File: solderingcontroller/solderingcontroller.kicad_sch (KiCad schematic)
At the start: 33 parts, among them J1 230V AC, Q3 BUZ11, Q4 BUZ11, SW1 HANDLE_DETECT, SW3 RotaryEncoder_Switch, T1 230/24, U1 ESP32-C3_SUPERMINI, U2 OLED LCD I2C, U3 16Bit I2C ADS1115 Module, U4 AMS1117-3.3, U6 VOM1271T, U7 4N25

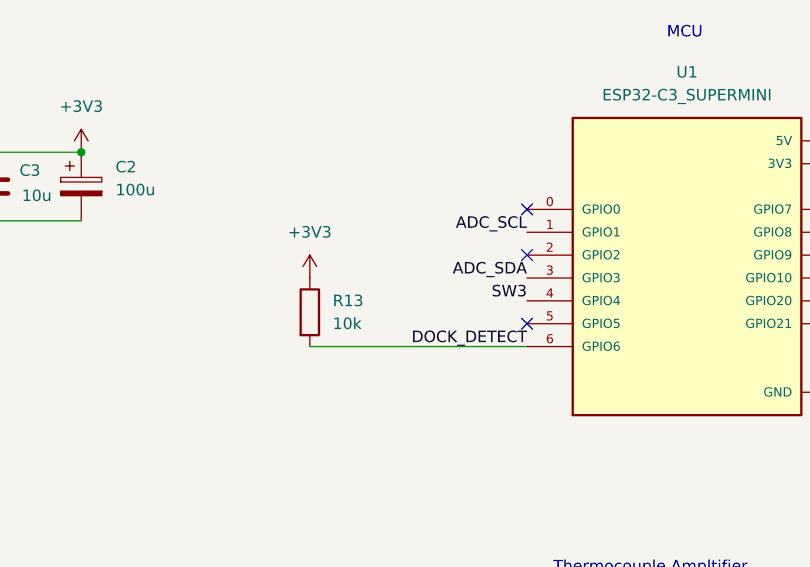
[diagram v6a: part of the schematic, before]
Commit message: Remove DOCK_DETECT PU
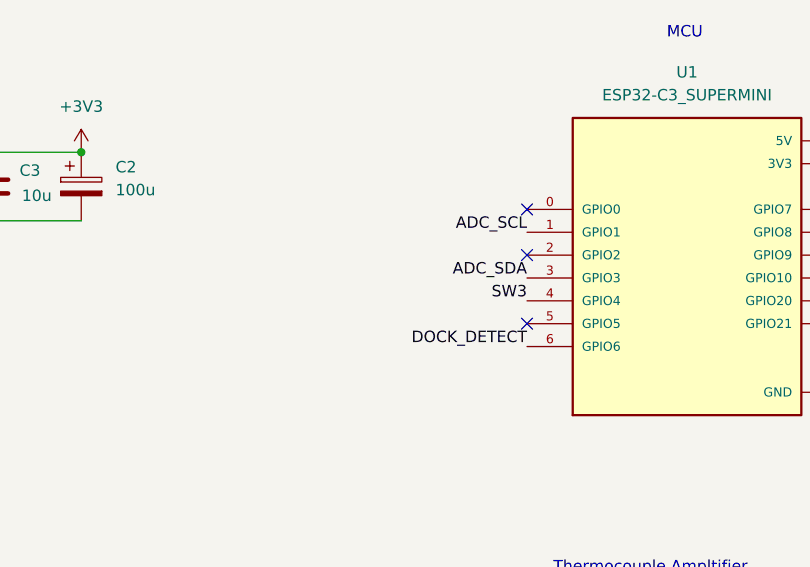
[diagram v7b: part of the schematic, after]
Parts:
- removed R13: 10k, symbol Device:R
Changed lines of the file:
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@@
 	(wire
 		(pts
-			(xy 86.36 52.07) (xy 110.49 52.07)
-		)
-		(stroke
-			(width 0)
-			(type default)
-		)
-	)
-	(wire
-		(pts
 			(xy 26.67 38.1) (xy 41.91 38.1)
 		)
@@
 	)
 	(symbol
-		(lib_id "Device:R")
-		(at 86.36 48.26 0)
-		(unit 1)
-		(exclude_from_sim no)
-		(in_bom yes)
-		(on_board yes)
-		(dnp no)
-		(fields_autoplaced yes)
-		(property "Reference" "R13"
-			(at 88.9 46.9899 0)
-			(effects
-				(font
-					(size 1.27 1.27)
-				)
-				(justify left)
-			)
-		)
-		(property "Value" "10k"
-			(at 88.9 49.5299 0)
-			(effects
-				(font
-					(size 1.27 1.27)
-				)
-				(justify left)
-			)
-		)
-		(property "Footprint" ""
-			(at 84.582 48.26 90)
-			(effects
-				(font
-					(size 1.27 1.27)
-				)
-				(hide yes)
-			)
-		)
-		(property "Datasheet" "~"
-			(at 86.36 48.26 0)
-			(effects
-				(font
-					(size 1.27 1.27)
-				)
-				(hide yes)
-			)
-		)
-		(property "Description" "Resistor"
-			(at 86.36 48.26 0)
-			(effects
-				(font
-					(size 1.27 1.27)
-				)
-				(hide yes)
-			)
-		)
-		(pin "2"
-		)
-		(pin "1"
-		)
-		(instances
-			(project "solderingcontroller"
-				(path "/9562c3ca-c9e5-4e2d-8a48-bcd20ff65be7"
-					(reference "R13")
-					(unit 1)
-				)
-			)
-		)
-	)
-	(symbol
 		(lib_id "power:GND")
 		(at 25.4 190.5 0)
@@
 					(unit 1)
 				)
-			)
-		)
-	)
-	(symbol
-		(lib_id "power:+3V3")
-		(at 86.36 44.45 0)
-		(unit 1)
-		(exclude_from_sim no)
-		(in_bom yes)
-		(on_board yes)
-		(dnp no)
-		(fields_autoplaced yes)
-		(property "Reference" "#PWR026"
-			(at 86.36 48.26 0)
-			(effects
-				(font
-					(size 1.27 1.27)
-				)
-				(hide yes)
-			)
-		)
-		(property "Value" "+3V3"
-			(at 86.36 39.37 0)
-			(effects
-				(font
-					(size 1.27 1.27)
-				)
-			)
-		)
-		(property "Footprint" ""
-			(at 86.36 44.45 0)
-			(effects
-				(font
-					(size 1.27 1.27)
-				)
-				(hide yes)
-			)
-		)
-		(property "Datasheet" ""
-			(at 86.36 44.45 0)
-			(effects
-				(font
-					(size 1.27 1.27)
-				)
-				(hide yes)
-			)
-		)
-		(property "Description" "Power symbol creates a global label with name \"+3V3\""
-			(at 86.36 44.45 0)
-			(effects
-				(font
-					(size 1.27 1.27)
-				)
-				(hide yes)
-			)
-		)
-		(pin "1"
-		)
-		(instances
-			(project "solderingcontroller"
-				(path "/9562c3ca-c9e5-4e2d-8a48-bcd20ff65be7"
-					(reference "#PWR026")
-					(unit 1)
-				)

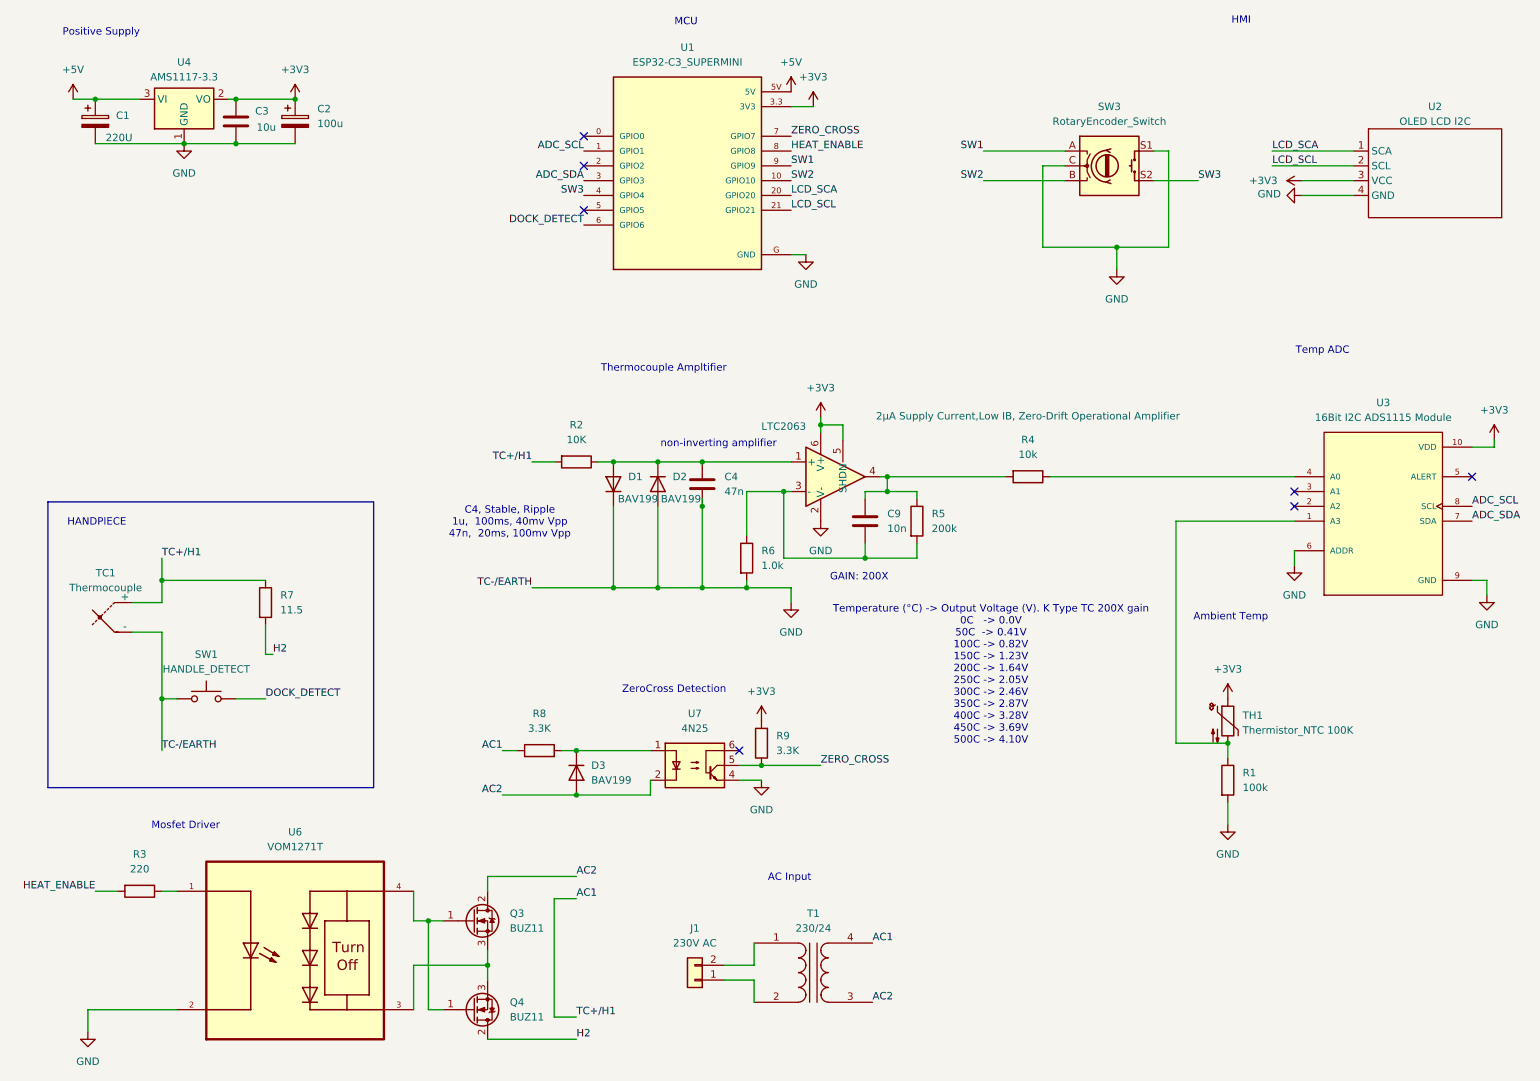
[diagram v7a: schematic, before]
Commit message: Add 230V -> 5V power supply
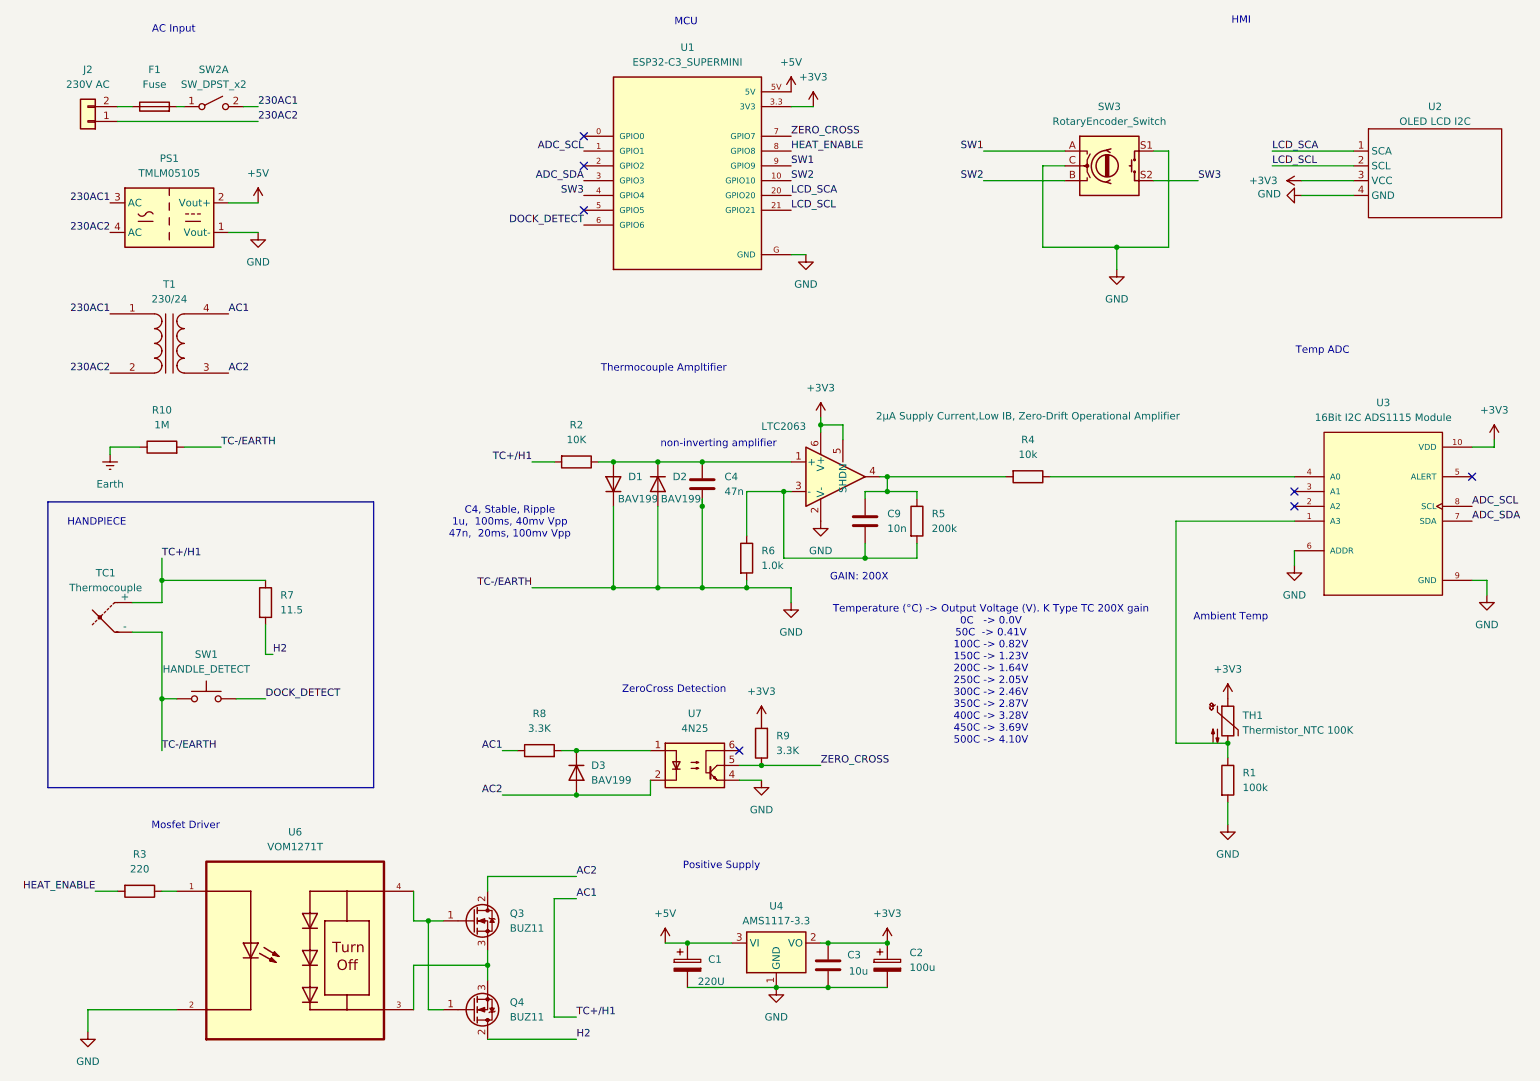
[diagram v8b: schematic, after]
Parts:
- removed J1: 230V AC, symbol Connector_Generic:Conn_01x02
- added F1: Fuse, symbol Device:Fuse
- added J2: 230V AC, symbol Connector_Generic:Conn_01x02
- added PS1: TMLM05105, Converter_ACDC:Converter_ACDC_TRACO_TMLM-05_THT, symbol Converter_ACDC:TMLM05105
- added R10: 1M, symbol Device:R
- added SW2: SW_DPST_x2, symbol Switch:SW_DPST_x2
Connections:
- net +5V: now also PS1.2 (Vout+)
- net GND: now also PS1.1 (Vout-), R10.2
- net 230AC1: now reaches T1.1 (AA)
- net 230AC1: now also PS1.3 (AC), SW2.2 (B)
- net 230AC2: now reaches T1.2 (AB)
- net 230AC2: now also J2.1 (Pin_1), PS1.4 (AC)
- new net: F1.1, J2.2 (Pin_2)
- new net: F1.2, SW2.1 (A)
- new net Earth: R10.1
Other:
- moved on the sheet: C1, C2, C3, T1, U4
